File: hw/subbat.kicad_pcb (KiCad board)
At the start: 2 copper layers, 100 x 100 mm, 188 parts, among them J1 Conn_01x02, J10 Conn_01x06_Male, J11 USB_Ax2, J12 USB_Ax2, J13 USB_Ax2, J14 Conn_01x02, J15 Conn_01x04_Male, J16 Conn_01x06_Male, J17 Conn_01x06_Male, J18 Conn_01x02, J19 USB_B_Micro, J2 Conn_01x02, J20 Conn_01x10_Male, J21 Conn_01x02, J22 Conn_01x02, J23 Conn_01x04_Male, J24 Conn_01x02, J3 Conn_01x02, J4 Conn_01x02, J5 Conn_01x02, J6 Conn_01x02, J7 Conn_01x06_Male, J8 Conn_01x02, J9 USB_Ax2, Q1 Q_NPN_BEC, Q10 Q_NPN_BEC, Q11 AOD403, Q12 AOD403, Q13 Q_NPN_BEC, Q14 AOD403, Q15 Q_NPN_BEC, Q16 Q_Photo_NPN_EC, Q17 Q_NPN_BEC, Q18 Q_PNP_BEC, Q2 Q_PMOS_GSD, Q9 AOD403, SW1 SW_Push, SW2 SW_Push, SW3 SW_Push, U1 ATMEGA328P-AU, U10 P82B715, U2 L7803, U3 ATTINY2313-20SU, U4 ATTINY13A-SSU, U5 LT6105, U6 LT6105, U7 LT6105, U8 LT6105, U9 LM393

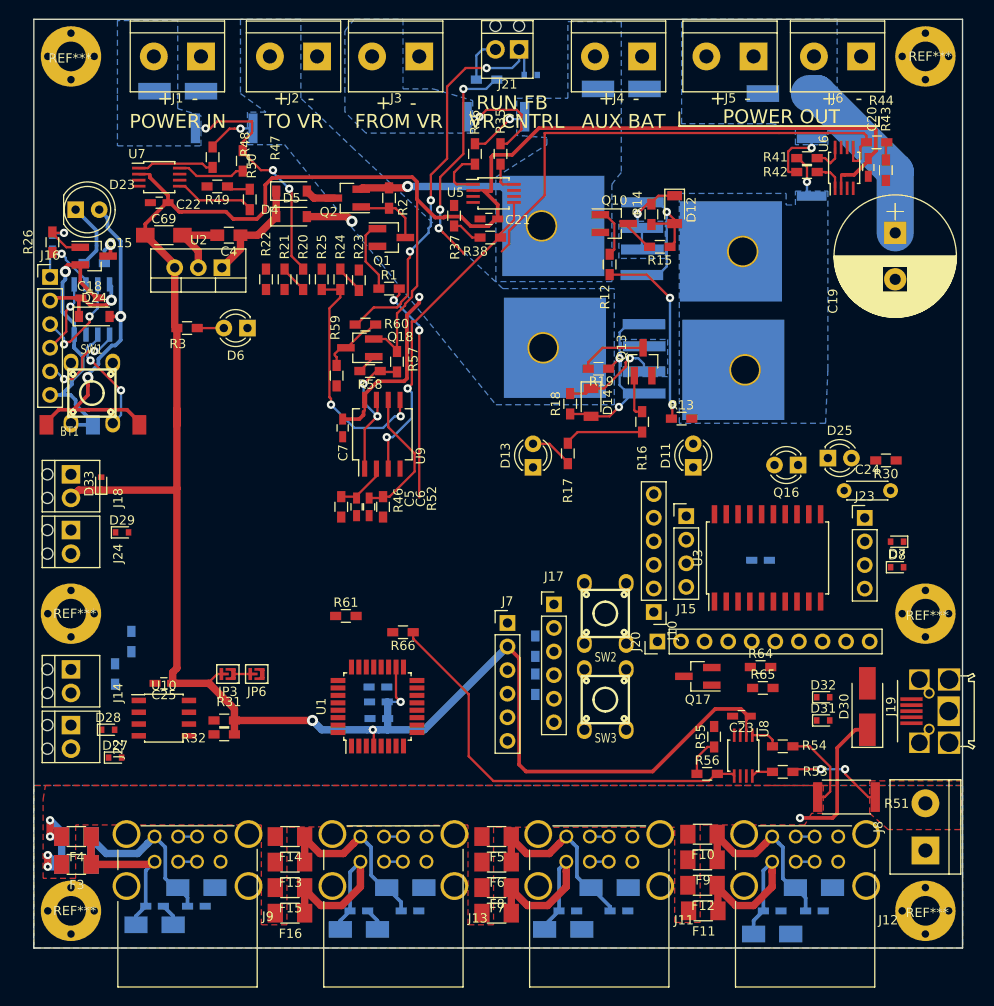
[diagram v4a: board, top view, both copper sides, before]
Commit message: Component rearrangement from scratch; DRC clear
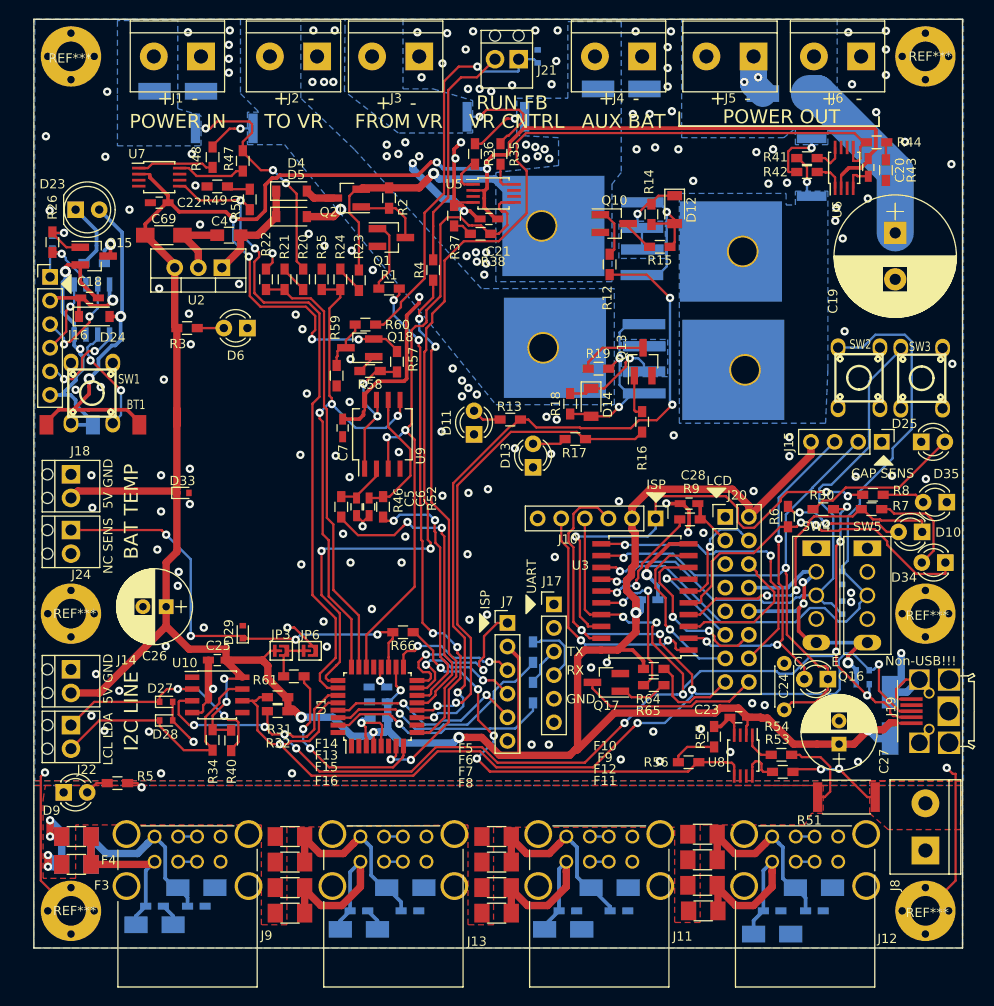
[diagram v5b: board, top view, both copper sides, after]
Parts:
- removed J23: Conn_01x04_Male, Pin_Headers:Pin_Header_Straight_1x04_Pitch2.54mm
- added C26: CP1_Small, Capacitors_ThroughHole:CP_Radial_D8.0mm_P2.50mm, F.Cu at (34.2, 83.2)
- added C27: CP1_Small, Capacitors_ThroughHole:CP_Radial_D8.0mm_P2.50mm, F.Cu at (106.7, 98.0)
- added C28: 1u, Capacitors_SMD:C_0603_HandSoldering, F.Cu at (90.5, 72.2)
- added D10: LED, LEDs:LED_D3.0mm, F.Cu at (115.7, 75.2)
- added D34: LED, LEDs:LED_D3.0mm, F.Cu at (118.2, 78.5)
- added D35: LED, LEDs:LED_D3.0mm, F.Cu at (118.3, 72.0)
- added D9: LED, LEDs:LED_D3.0mm, F.Cu at (23.2, 103.2)
- added R5: 2.2k, Resistors_SMD:R_0603_HandSoldering, F.Cu at (29.0, 102.2)
- added R6: 2.2k, Resistors_SMD:R_0603_HandSoldering, F.Cu at (101.2, 73.5)
- added R7: 2.2k, Resistors_SMD:R_0603_HandSoldering, F.Cu at (110.2, 72.8)
- added R8: 2.2k, Resistors_SMD:R_0603_HandSoldering, F.Cu at (110.3, 71.2)
- added R9: 100k, Resistors_SMD:R_0603_HandSoldering, F.Cu at (90.7, 73.8)
- added SW4: SW_SPDT_WITH_SHIELD, components:SW_SPDT_WITH_SHILD, F.Cu at (104.2, 77.0)
- added SW5: SW_SPDT_WITH_SHIELD, components:SW_SPDT_WITH_SHILD, F.Cu at (109.8, 77.0)
- D30, D31, D32, D7, D8: moved to B.Cu
- J20: value Conn_01x10_Male -> Conn_02x08_Odd_Even; footprint Pin_Headers:Pin_Header_Straight_1x10_Pitch2.54mm -> Pin_Headers:Pin_Header_Straight_2x08_Pitch2.54mm
- R34, R4, R40: moved to F.Cu
- moved SW3 48.6 mm to (115.6, 58.6)
- moved SW2 37.3 mm to (108.8, 58.6)
- moved C24 24.5 mm to (100.8, 94.3), turned to 90 degrees
- moved D11 23.9 mm to (67.4, 64.7)
- moved Q16 23.3 mm to (105.5, 91.0)
- moved J15 22.5 mm to (111.3, 65.5), turned to 270 degrees
- moved R4 21.3 mm to (63.0, 47.0), turned to 270 degrees
- moved R13 18.5 mm to (71.3, 63.1), turned to 180 degrees
- moved D29 16.9 mm to (42.5, 86.0), turned to 90 degrees
- moved J20 15.3 mm to (94.5, 73.6), turned to 0 degrees
- moved R40 15.1 mm to (41.2, 97.7)
- moved U3 13.9 mm to (85.8, 82.2), turned to 180 degrees
- moved C10 12.7 mm to (86.2, 82.5)
- moved R34 12.7 mm to (39.2, 97.6), turned to 270 degrees
- moved R65 11.8 mm to (86.8, 91.7)
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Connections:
- C10 pad 1: VCOM -> +5V
- C11 pad 2: GND -> BUSGND
- C12 pad 2: GND -> BUSGND
- C13 pad 2: GND -> BUSGND
- C14 pad 2: GND -> BUSGND
- C15 pad 2: GND -> BUSGND
- C16 pad 2: GND -> BUSGND
- C8 pad 2: GND -> BUSGND
- C9 pad 2: GND -> BUSGND
- D15 pad 2: GND -> BUSGND
- D16 pad 2: GND -> BUSGND
- D17 pad 2: GND -> BUSGND
- D18 pad 2: GND -> BUSGND
- D19 pad 2: GND -> BUSGND
- D20 pad 2: GND -> BUSGND
- D21 pad 2: GND -> BUSGND
- D22 pad 2: GND -> BUSGND
- D30 pad 1: VCOM -> +5V
- D7 pad 1: /WaterLevel/PREFER_DISCHG -> /WaterLevel/ALLOW_DISCHG
- D8 pad 1: /WaterLevel/ALLOW_DISCHG -> /WaterLevel/PREFER_DISCHG
- J10 pad 2: VCOM -> +5V
- J11 pad 4: GND -> BUSGND
- J11 pad 8: GND -> BUSGND
- J11 pad 9: GND -> BUSGND
- J12 pad 4: GND -> BUSGND
- J12 pad 8: GND -> BUSGND
- J12 pad 9: GND -> BUSGND
- J13 pad 4: GND -> BUSGND
- J13 pad 8: GND -> BUSGND
- J13 pad 9: GND -> BUSGND
- J15 pad 4: VCOM -> +5V
- J19 pad 1: VCOM -> +5V
- J20 pad 1: Net-(J20-Pad1) -> GND
- J20 pad 10: /WaterLevel/LCD_D7 -> GND
- J20 pad 2: Net-(J20-Pad2) -> +5V
- J20 pad 3: GND -> Net-(C28-Pad1)
- J20 pad 4: VCOM -> /WaterLevel/LCD_RS
- J20 pad 5: /WaterLevel/LCD_E -> GND
- J20 pad 6: /WaterLevel/LCD_RS -> /WaterLevel/LCD_E
- J20 pad 7: /WaterLevel/LCD_D4 -> GND
- J20 pad 8: /WaterLevel/LCD_D5 -> GND
- J20 pad 9: /WaterLevel/LCD_D6 -> GND
- J8 pad 1: GND -> BUSGND
- J9 pad 4: GND -> BUSGND
- J9 pad 8: GND -> BUSGND
- J9 pad 9: GND -> BUSGND
- Q17 pad 3: Net-(J20-Pad2) -> Net-(J20-Pad16)
- R64 pad 1: VCOM -> +5V
- R64 pad 2: Net-(J20-Pad1) -> Net-(J20-Pad15)
- U3 pad 15: /WaterLevel/CHARGE -> /WaterLevel/LCD_CONTRAST
- U3 pad 2: Net-(U3-Pad2) -> /WaterLevel/CHARGE
- U3 pad 20: VCOM -> +5V
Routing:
- net GND: track 44.8 -> 204.9 mm, vias 1 -> 189
- net SDA: track 0.00 -> 153.4 mm, vias 0 -> 12
- net SCL: track 0.00 -> 139.0 mm, vias 0 -> 6
- net +5V: track 298.0 -> 411.0 mm, vias 3 -> 14
- net /WaterLevel/PREFER_DISCHG: track 0.00 -> 75.1 mm, vias 0 -> 1
- net /IOUT_SENS: track 54.6 -> 122.5 mm, vias 0 -> 2
- net /ISYS_SENS: track 8.68 -> 71.5 mm, vias 0 -> 2
- net /WaterLevel/ALLOW_DISCHG: track 0.00 -> 61.7 mm, vias 0 -> 1
- net /WaterLevel/SENS: track 0.00 -> 59.3 mm, vias 0 -> 2
- net /SW_BAT: track 20.7 -> 77.6 mm, vias 2 -> 4
- net /WaterLevel/MISO: track 0.00 -> 50.4 mm, vias 0 -> 3
- net /BAT_TEMP_SENS: track 0.00 -> 49.1 mm, vias 0 -> 4
- net /VS_SENSE_ADC: track 0.00 -> 47.1 mm
- net /SW_VS: track 8.58 -> 52.5 mm, vias 0 -> 2
- net /WaterLevel/CHARGE: track 0.00 -> 39.9 mm, vias 0 -> 3
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- added copper zone on B.Cu, net BUSGND
- added copper zone on F.Cu, net BUSGND
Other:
- board text added: "5V GND"
- board text added: "BAT TEMP"
- board text added: "C"
- board text added: "CAP SENS"
- board text added: "E"
- board text added: "GND"
- board text added: "I2C LINE"
- board text added: "ISP"
- board text added: "LCD"
- board text added: "LCL LDA"
- board text added: "Longer Shorter"
- board text added: "NC SENS"
- board text added: "Non-USB!!!"
- board text added: "RX"
- board text added: "TX"
- board text added: "UART"

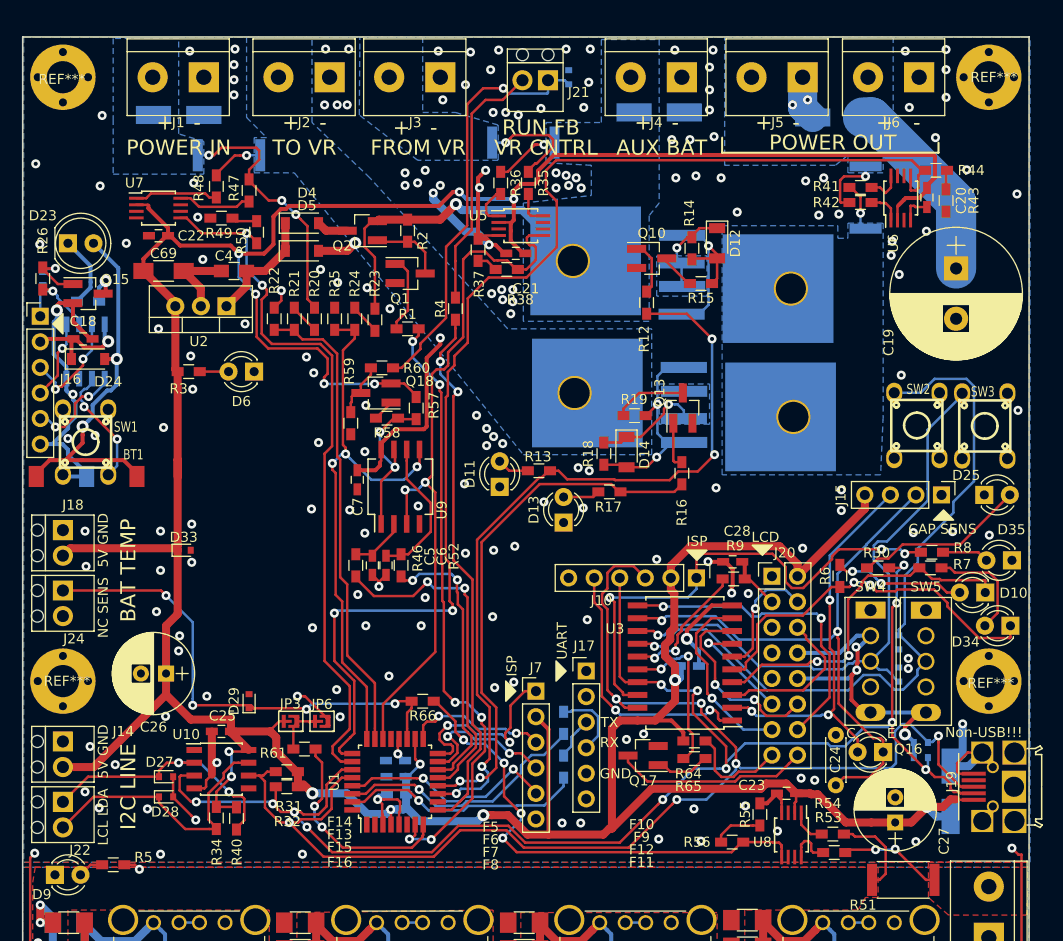
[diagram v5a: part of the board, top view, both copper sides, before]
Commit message: Added resettable fuses; DRC clear
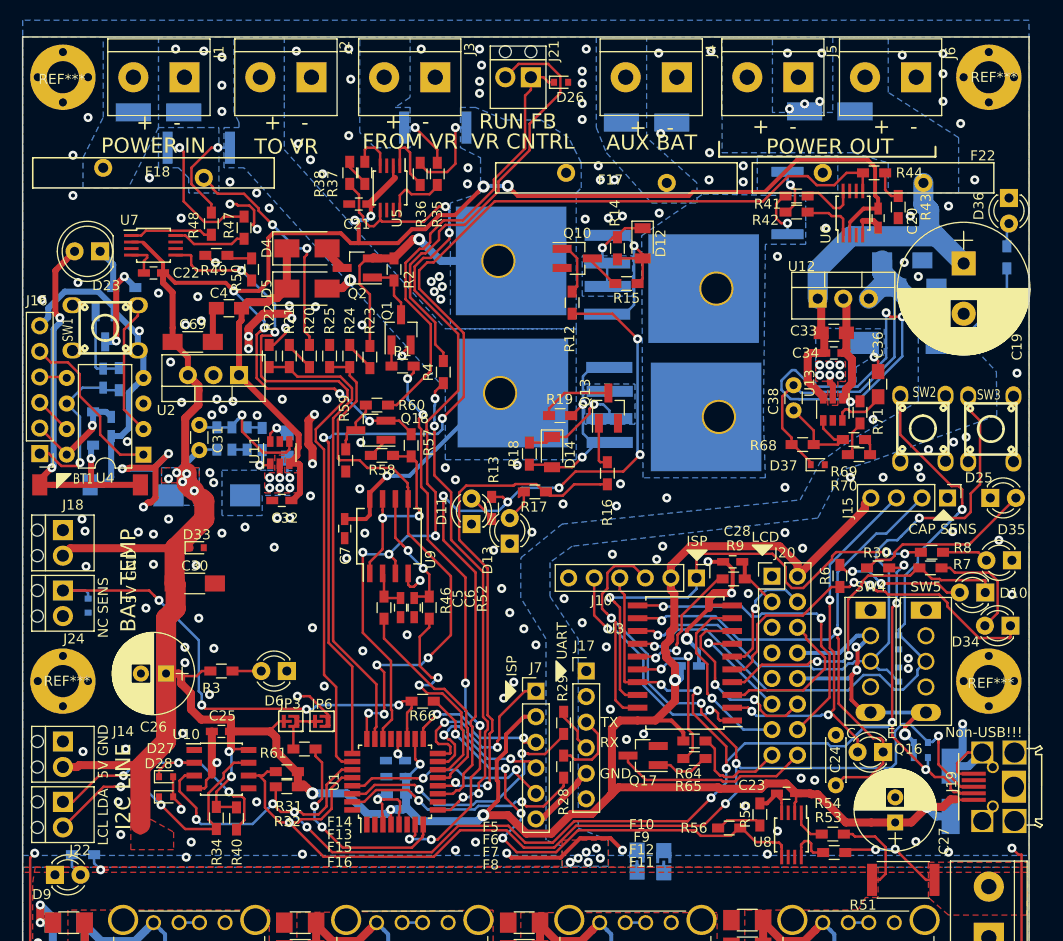
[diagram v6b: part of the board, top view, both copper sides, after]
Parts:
- added C29: 0.1u 50V, Capacitors_SMD:C_0805_HandSoldering, B.Cu at (46.3, 60.6)
- added C30: 10u, Capacitors_SMD:C_1206_HandSoldering, F.Cu at (37.1, 74.3)
- added C31: 75p, Capacitors_ThroughHole:C_Disc_D3.0mm_W1.6mm_P2.50mm, F.Cu at (37.5, 61.0)
- added C32: 1u, Capacitors_SMD:C_0603_HandSoldering, F.Cu at (45.8, 66.0)
- added C33: 4.7u 50V, Capacitors_SMD:C_0805_HandSoldering, F.Cu at (100.6, 49.4)
- added C34: 1u, Capacitors_SMD:C_0603_HandSoldering, F.Cu at (100.6, 51.4)
- added C35: 10u, Capacitors_SMD:C_1206_HandSoldering, B.Cu at (107.4, 42.2)
- added C36: 0.1u 50V, Capacitors_SMD:C_0805_HandSoldering, F.Cu at (105.0, 54.5)
- added C37: 10u, Capacitors_SMD:C_1206_HandSoldering, B.Cu at (108.8, 44.8)
- added C38: 75p, Capacitors_ThroughHole:C_Disc_D3.0mm_W1.6mm_P2.50mm, F.Cu at (96.6, 54.6)
- added D36: LED, LEDs:LED_D3.0mm, F.Cu at (118.0, 36.0)
- added D37: ESD5Z5.0T1G, Diodes_SMD:D_SOD-523, F.Cu at (99.0, 62.5)
- added F17: 9A hold, 18A trip, components:POLYSWITCH_W24_P10, F.Cu at (79.0, 34.0)
- added F18: 9A hold, 18A trip, components:POLYSWITCH_W24_P10, F.Cu at (33.0, 33.5)
- added F22: 9A hold, 18A trip, components:POLYSWITCH_W24_P10, F.Cu at (104.5, 34.0)
- added JP4: Jumper_NO_Small, components:SolderJumper_L, B.Cu at (81.0, 101.8)
- added JP5: Jumper_NO_Small, components:SolderJumper_L, B.Cu at (83.7, 101.8)
- added L1: 22u, components:Choke_SMD_7.3x7.3_H3.5_handsoldering, B.Cu at (38.3, 65.5)
- added L2: 22u, components:Choke_SMD_7.3x7.3_H3.5_handsoldering, B.Cu at (107.4, 50.4)
- added R10: 1k, Resistors_SMD:R_0603_HandSoldering, B.Cu at (43.8, 60.0)
- added R11: 100k, Resistors_SMD:R_0603_HandSoldering, B.Cu at (39.3, 59.9)
- added R62: 10k, Resistors_SMD:R_0603_HandSoldering, B.Cu at (40.8, 59.9)
- added R63: 2.2k, Resistors_SMD:R_0603_HandSoldering, B.Cu at (42.3, 59.9)
- added R67: 2.2k, Resistors_SMD:R_0603_HandSoldering, B.Cu at (117.8, 41.9)
- added R68: 100k, Resistors_SMD:R_0603_HandSoldering, F.Cu at (97.5, 60.5)
- added R69: 10k, Resistors_SMD:R_0603_HandSoldering, F.Cu at (102.6, 60.0)
- added R70: 2.2k, Resistors_SMD:R_0603_HandSoldering, F.Cu at (103.1, 61.5)
- added R71: 1k, Resistors_SMD:R_0603_HandSoldering, F.Cu at (103.2, 57.3)
- added U11: TPS54202, TO_SOT_Packages_SMD:SOT-23-6, F.Cu at (45.5, 61.3)
- added U12: L7803, TO_SOT_Packages_THT:TO-220-3_Vertical, F.Cu at (99.0, 46.0)
- added U13: TPS54202, TO_SOT_Packages_SMD:SOT-23-6, F.Cu at (100.5, 57.0)
- C18, D24, D29, Q15, R26, R5: moved to B.Cu
- C4: value 4.7u -> 4.7u 50V
- D26, R28, R29: moved to F.Cu
- D4, D5: footprint Diodes_SMD:D_SOD-123 -> Diodes_SMD:D_SMA
- U4: footprint Housings_SOIC:SOIC-8_3.9x4.9mm_Pitch1.27mm -> Housings_DIP:DIP-8_W7.62mm; moved to F.Cu
- moved D6 29.9 mm to (46.2, 83.0)
- moved R3 29.9 mm to (39.8, 83.0)
- moved D29 18.6 mm to (26.5, 76.5), turned to 270 degrees
- moved R38 18.3 mm to (52.5, 33.5), turned to 270 degrees
- moved C21 16.4 mm to (53.4, 36.6)
- moved J16 13.7 mm to (21.7, 61.4), turned to 180 degrees
- moved R37 13.6 mm to (54.0, 33.5)
- moved U5 13.5 mm to (56.5, 35.0), turned to 270 degrees
- moved R26 12.6 mm to (29.6, 54.0)
- moved U4 11.8 mm to (32.0, 61.5), turned to 180 degrees
- moved C17 11.6 mm to (28.0, 53.9)
- moved SW1 11.5 mm to (28.2, 48.9), turned to 90 degrees
- moved C18 9.14 mm to (28.8, 58.7), turned to 270 degrees
- moved R35 9.09 mm to (61.2, 33.6)
- moved R33 8.88 mm to (61.0, 29.0)
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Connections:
- net Net-(C4-Pad1) renamed /Power5V/REG_IN
- D1 pad 1: /VS -> /VSIN
- D2 pad 1: /VA -> /VA2
- J1 pad 2: /VS -> /VSIN
- J4 pad 2: /VA -> /VA2
- R39 pad 1: /VOUT2 -> /VOUTM
- R42 pad 1: /VOUT2 -> /VOUTM
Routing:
- net GND: track 204.9 -> 299.8 mm, vias 189 -> 213
- net VCOM: track 23.6 -> 78.1 mm, vias 5 -> 11
- net /Power5V/REG_IN: track 11.8 -> 32.2 mm
- net Net-(J21-Pad2): track 25.4 -> 43.7 mm
- net Net-(C31-Pad2): track 0.00 -> 14.7 mm, vias 0 -> 1
- net +5V: track 411.0 -> 423.9 mm, vias 14 -> 21
- net /CC_CTRL: track 34.1 -> 21.7 mm, vias 2 -> 0
- net /VOUT2: track 26.1 -> 38.0 mm, vias 1 -> 0
- net /ICHARGE_SENS: track 71.1 -> 83.0 mm, vias 2 -> 5
- net /VS: track 26.0 -> 37.1 mm
- net Net-(C38-Pad2): track 0.00 -> 10.5 mm
- net /IOUT_SENS: track 122.5 -> 113.9 mm
- net /SingleButtonRemocon/LED_OUT: track 9.47 -> 17.0 mm
- net /WaterLevel/PREFER_DISCHG: track 75.1 -> 67.8 mm, vias 1 -> 2
- net /VS2: track 28.5 -> 35.8 mm
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- added copper zone on B.Cu, net +5V
- added copper zone on F.Cu, net +5V
- added copper zone on B.Cu, net /Power5V/VSW
- added copper zone on F.Cu, net /Power5V/VSW
- added copper zone on B.Cu, net /Power5V/VSW2
- added copper zone on F.Cu, net /Power5V/VSW2
- added copper zone on B.Cu, net /VA2
- added copper zone on B.Cu, net /VOUTM
- added copper zone on B.Cu, net /VSIN
- added copper zone on B.Cu, net VCOM
